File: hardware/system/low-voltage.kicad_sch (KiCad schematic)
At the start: 15 parts, among them M10 Buck 5 V >=2 A, M11 Motion carrier, M12 TB6600 1/8 step, M13 Stepper motor, M14 5 V relay module, M15 HOME bottom limit NC, M16 TOP limit NC, M17 Touch plate + clip on bit, M18 Foot pedal NO, M19 STOP flush NO, M20 Panel carrier, M21 Guition JC4827W543C, M22 MPG ZS80 100 PPR 5 V, M23 Panel buttons + rough/fine, M24 ROUTER LED

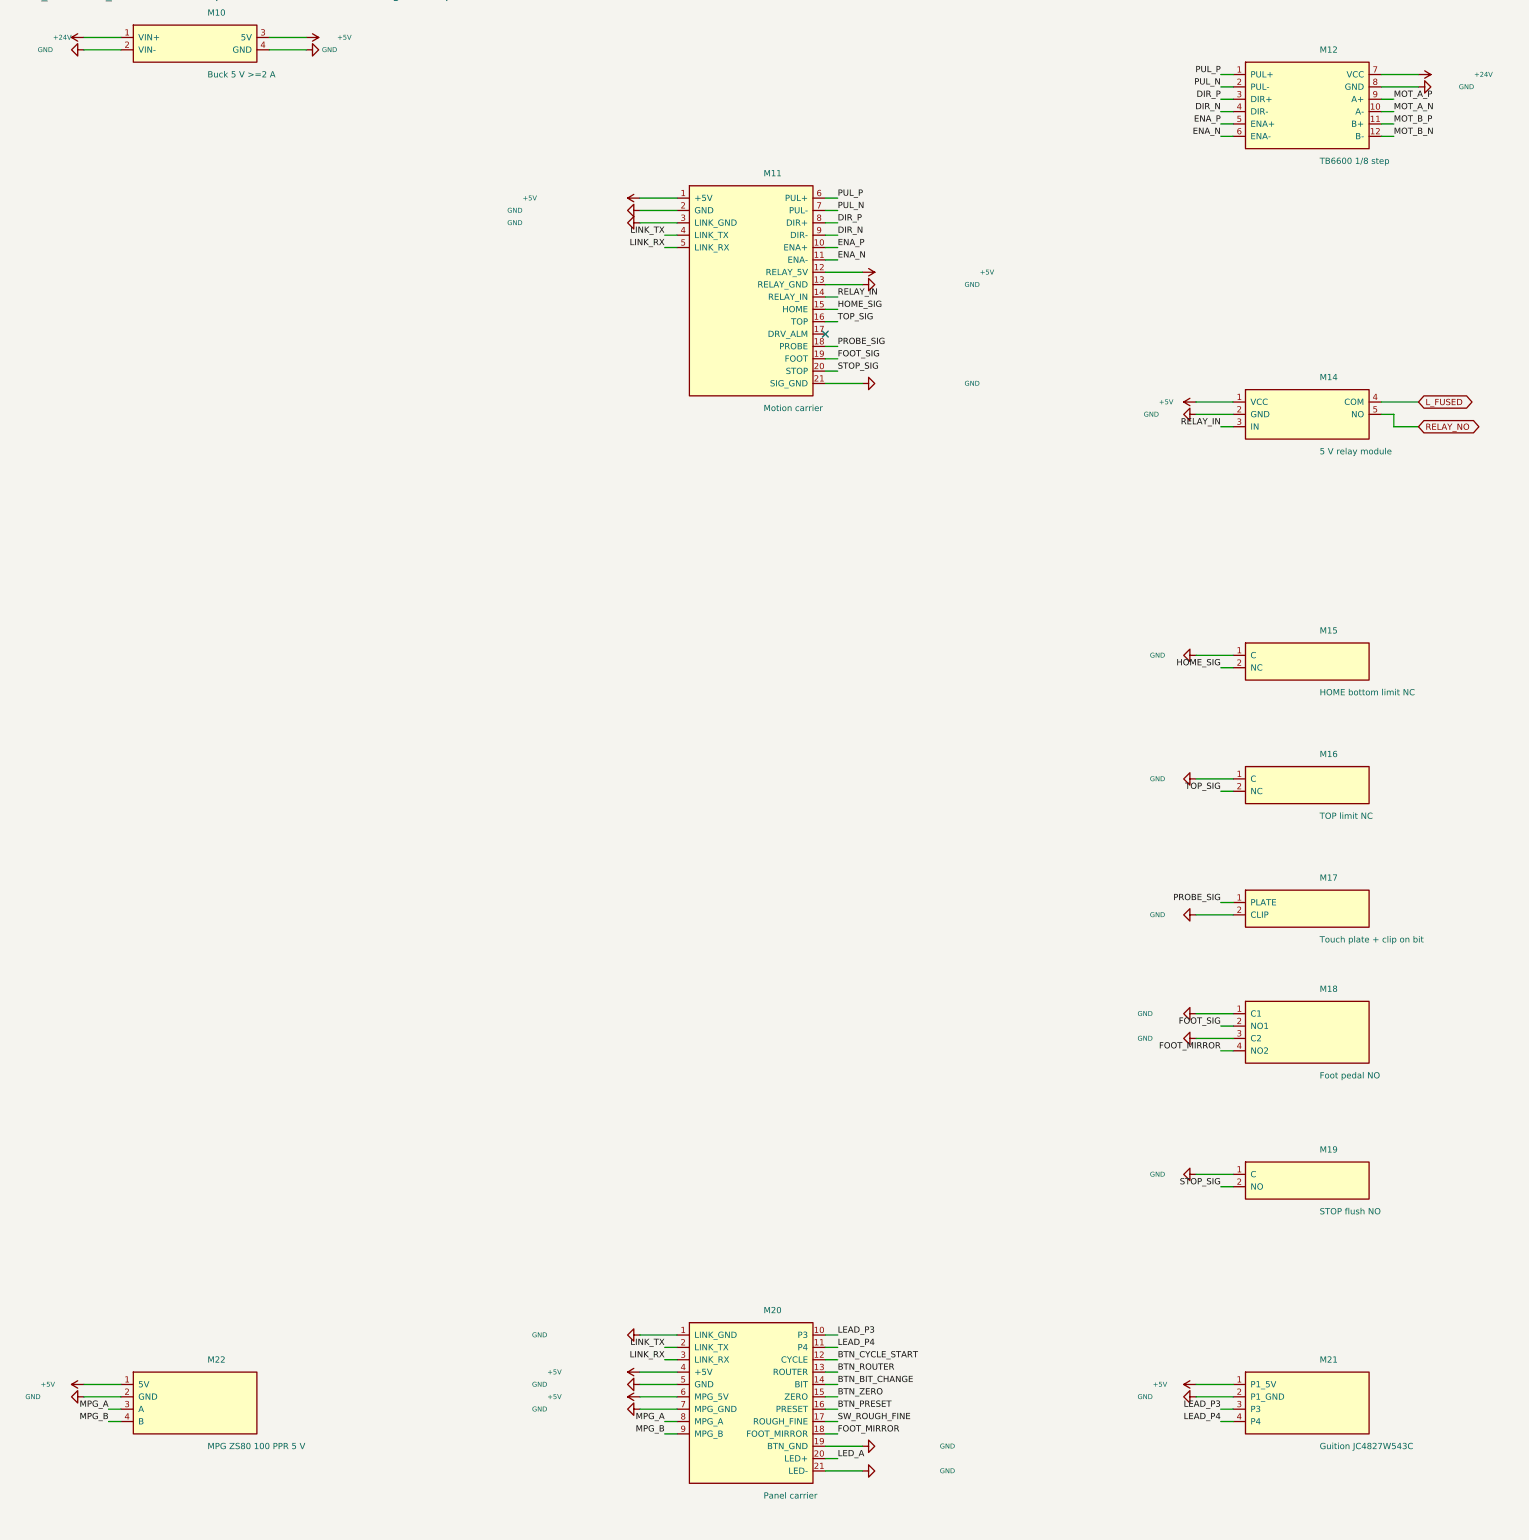
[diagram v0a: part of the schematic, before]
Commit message: fix(hardware): stop power-net arrows overlapping the plain pin below them
Review round 1 found a Critical, widespread legibility failure on the
low-voltage sheet: any box_symbol() row where a POWER_NET pin (GND/+5V) sits
directly above a plain-net pin had the plain label's text overlapped by the
power flag's own arrow/ground-symbol graphic, not just its Value text (already
covered by PowerNetLegibilityTest). Mechanism: the power flag's shape is
centred on its own row and reaches about half of box_symbol()'s 2.54mm row
pitch either side of it; a plain label is justified against the *bottom* of
its anchor (label()), so it grows upward, toward the row above. Both reaches
meet almost exactly at the row boundary by construction - stub length only
moves things along the wire, not perpendicular to it, so the earlier
"give globals the longer stub" fix could not touch this.

kisch.py: place() gains an opt-in `jog` parameter - {pin: extra} inserts a
perpendicular step into that one pin's wire before its label/flag. Every
existing caller that omits it draws the exact wire it always did (see
JogTest.test_omitting_jog_draws_the_same_single_straight_wire_as_before and
test_zero_jog_also_draws_a_single_straight_wire). Added JogTest: reproduces
the collision (both left- and right-side box_symbol() orientations, using the
real "power:GND" polyline geometry) and confirms a jog clears it.

hardware/tools/system.py: power_plain_jogs() computes the needed jog
automatically from BOXES + the nets being placed for every box - not
hand-tuned per occurrence. A power pin whose own row above is empty or plain
jogs itself up, away from the plain pin below. When its own above is another
power pin (no margin proven there to spare), the plain run below it - every
consecutive plain pin down to the next power pin or the end of the list -
cascades down together instead, preserving their mutual spacings exactly
while only shrinking the one gap already proven safe elsewhere in this file.
An earlier, si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
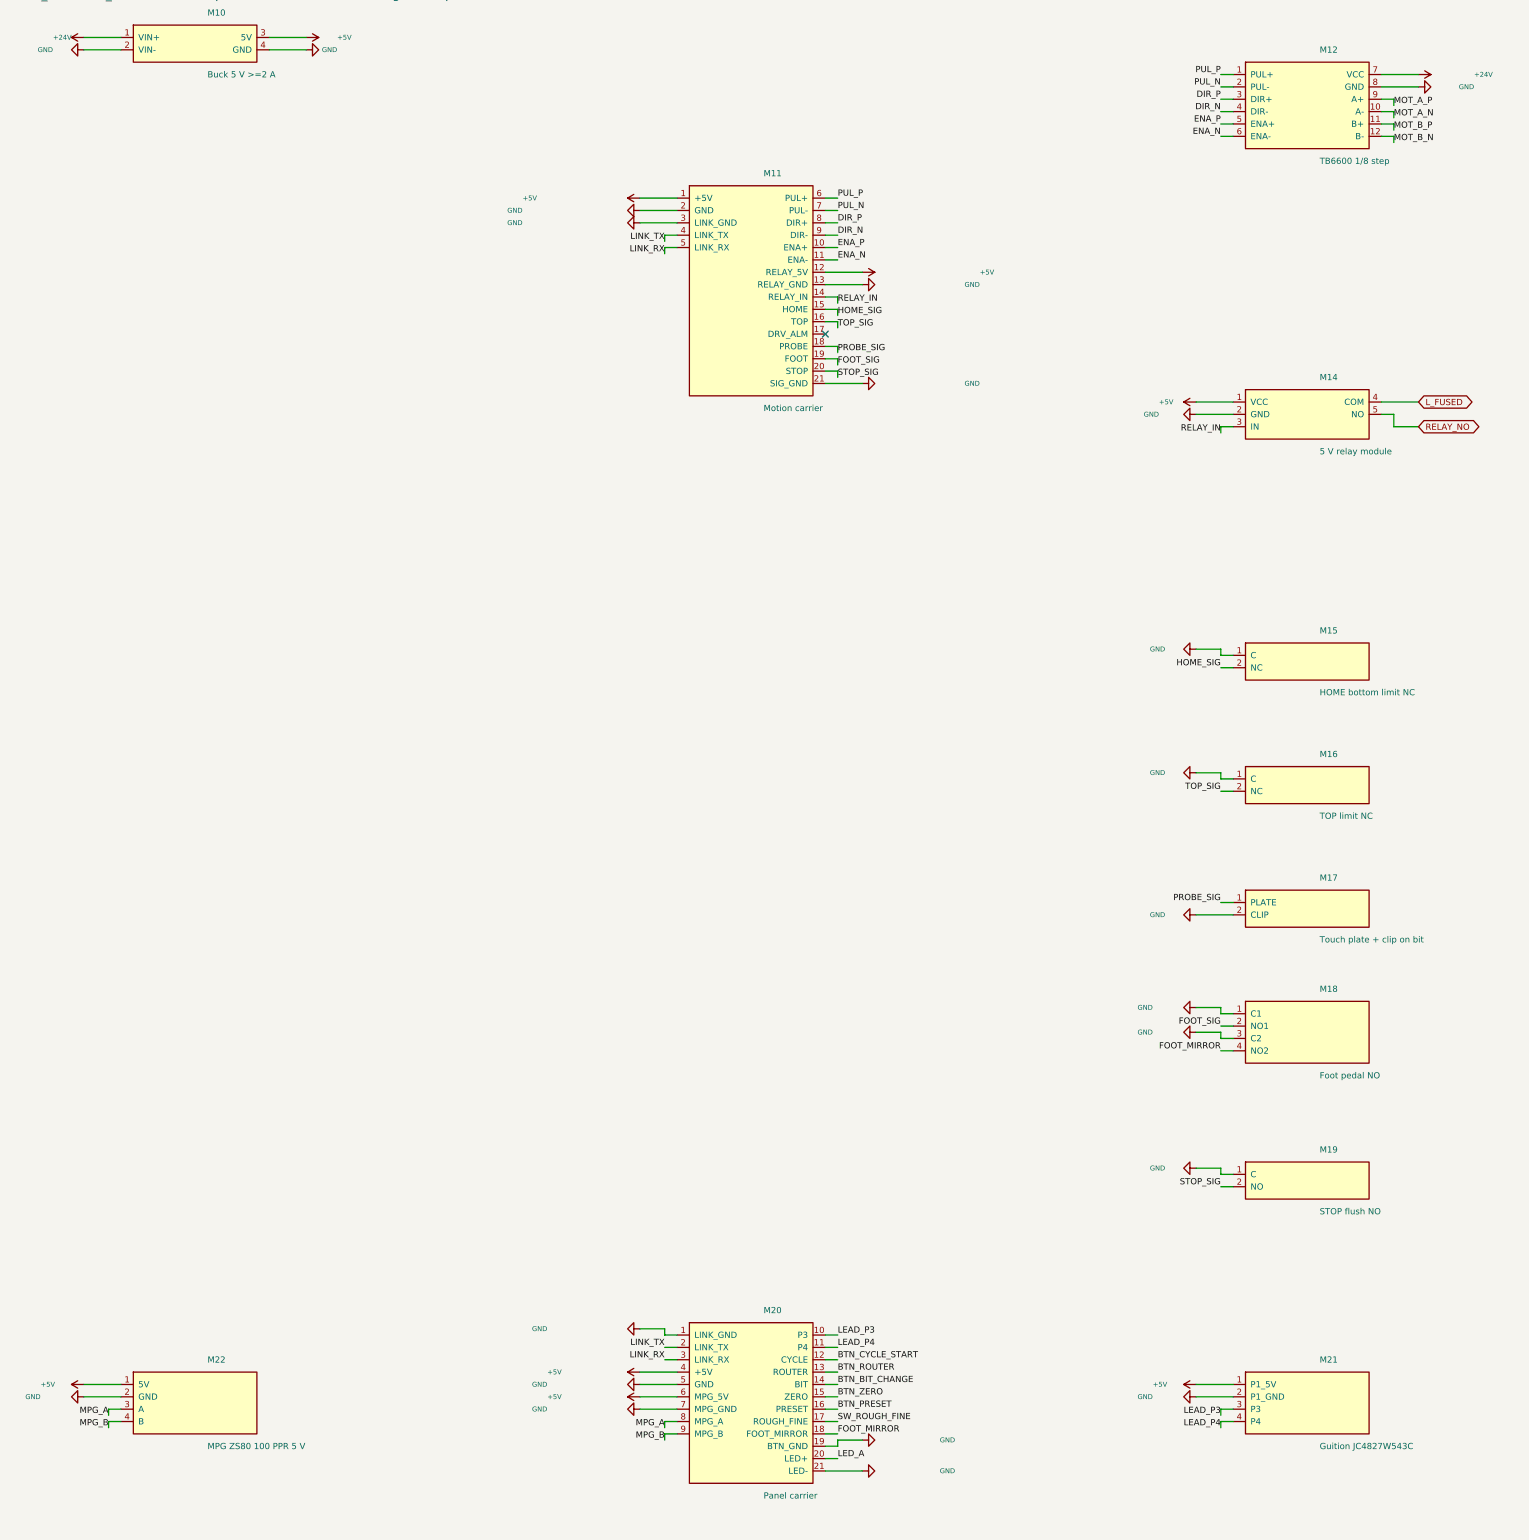
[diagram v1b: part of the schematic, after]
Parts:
- removed M13: Stepper motor, symbol routerlift:STEPPER
- added M19: STOP flush NO, symbol routerlift:STOP_BUTTON
- M13: renamed from M15; value HOME bottom limit NC -> Stepper motor; symbol routerlift:LIMIT_SWITCH_NC -> routerlift:STEPPER
- M15: renamed from M19; value STOP flush NO -> HOME bottom limit NC; symbol routerlift:STOP_BUTTON -> routerlift:LIMIT_SWITCH_NC
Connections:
- net GND: now also M19.1 (C); no longer M13.1 (C)
- net HOME_SIG: now also M15.2 (NC); no longer M13.2 (NC)
- net MOT_A_N: now also M13.2 (A-)
- net MOT_A_P: now also M13.1 (A+)
- net MOT_B_N: now also M13.4 (B-)
- net MOT_B_P: now also M13.3 (B+)
- net STOP_SIG: now also M19.2 (NO); no longer M15.2 (NO)
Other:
- moved on the sheet: M15

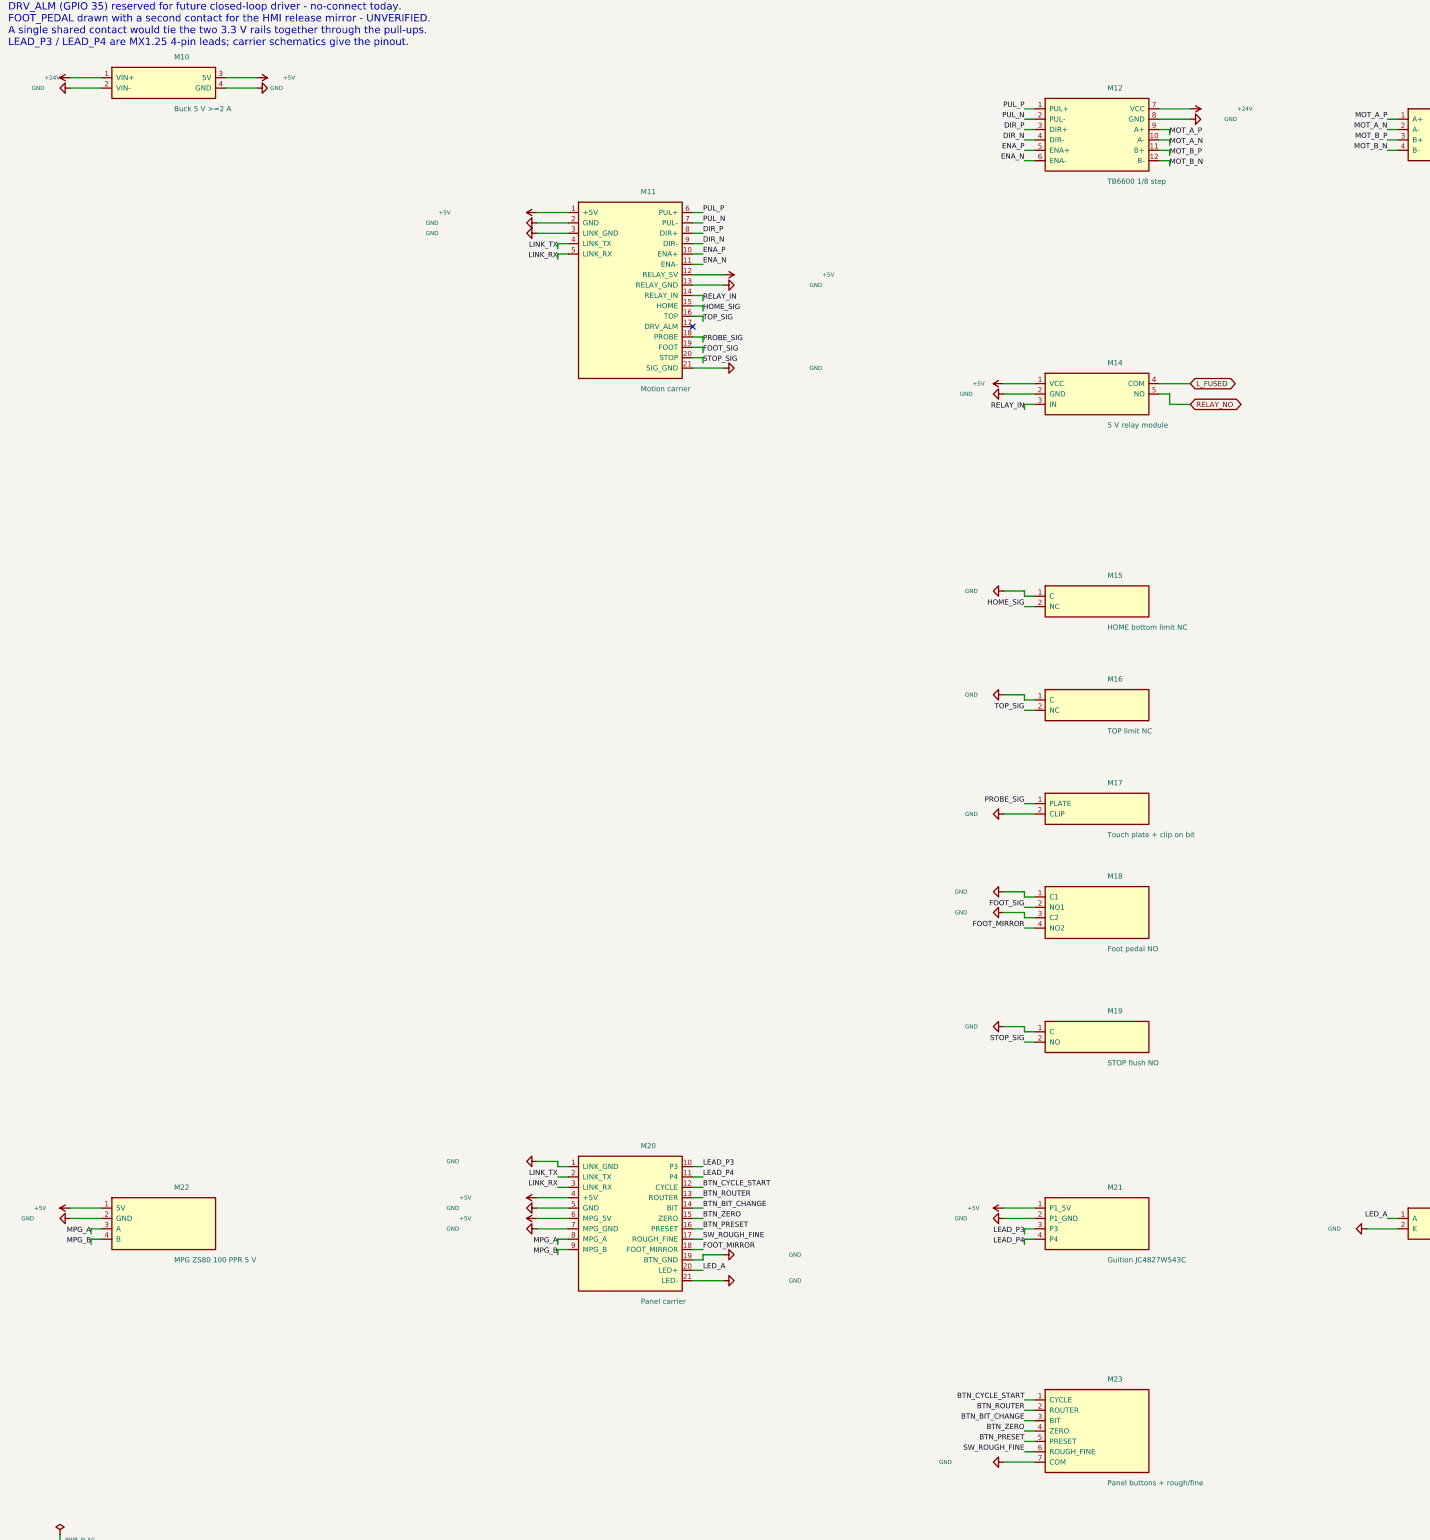
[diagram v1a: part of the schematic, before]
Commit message: fix(hardware): regenerate schematics, symbol library and PDFs
Regenerated output of the preceding fix-wave commits (contactor topology,
devkit pin order, field_gap/arrow-legibility fixes, 74LVC14 fields,
zero-length wire removal). ERC clean (0 violations on all three projects)
and check_pins reports 0 mismatches.

Co-Authored-By: Claude Opus 5 (1M context) <noreply@anthropic.com>
Claude-Session: https://claude.ai/code/session_01N1nWXzYgvFT6pqfHGhLK6P
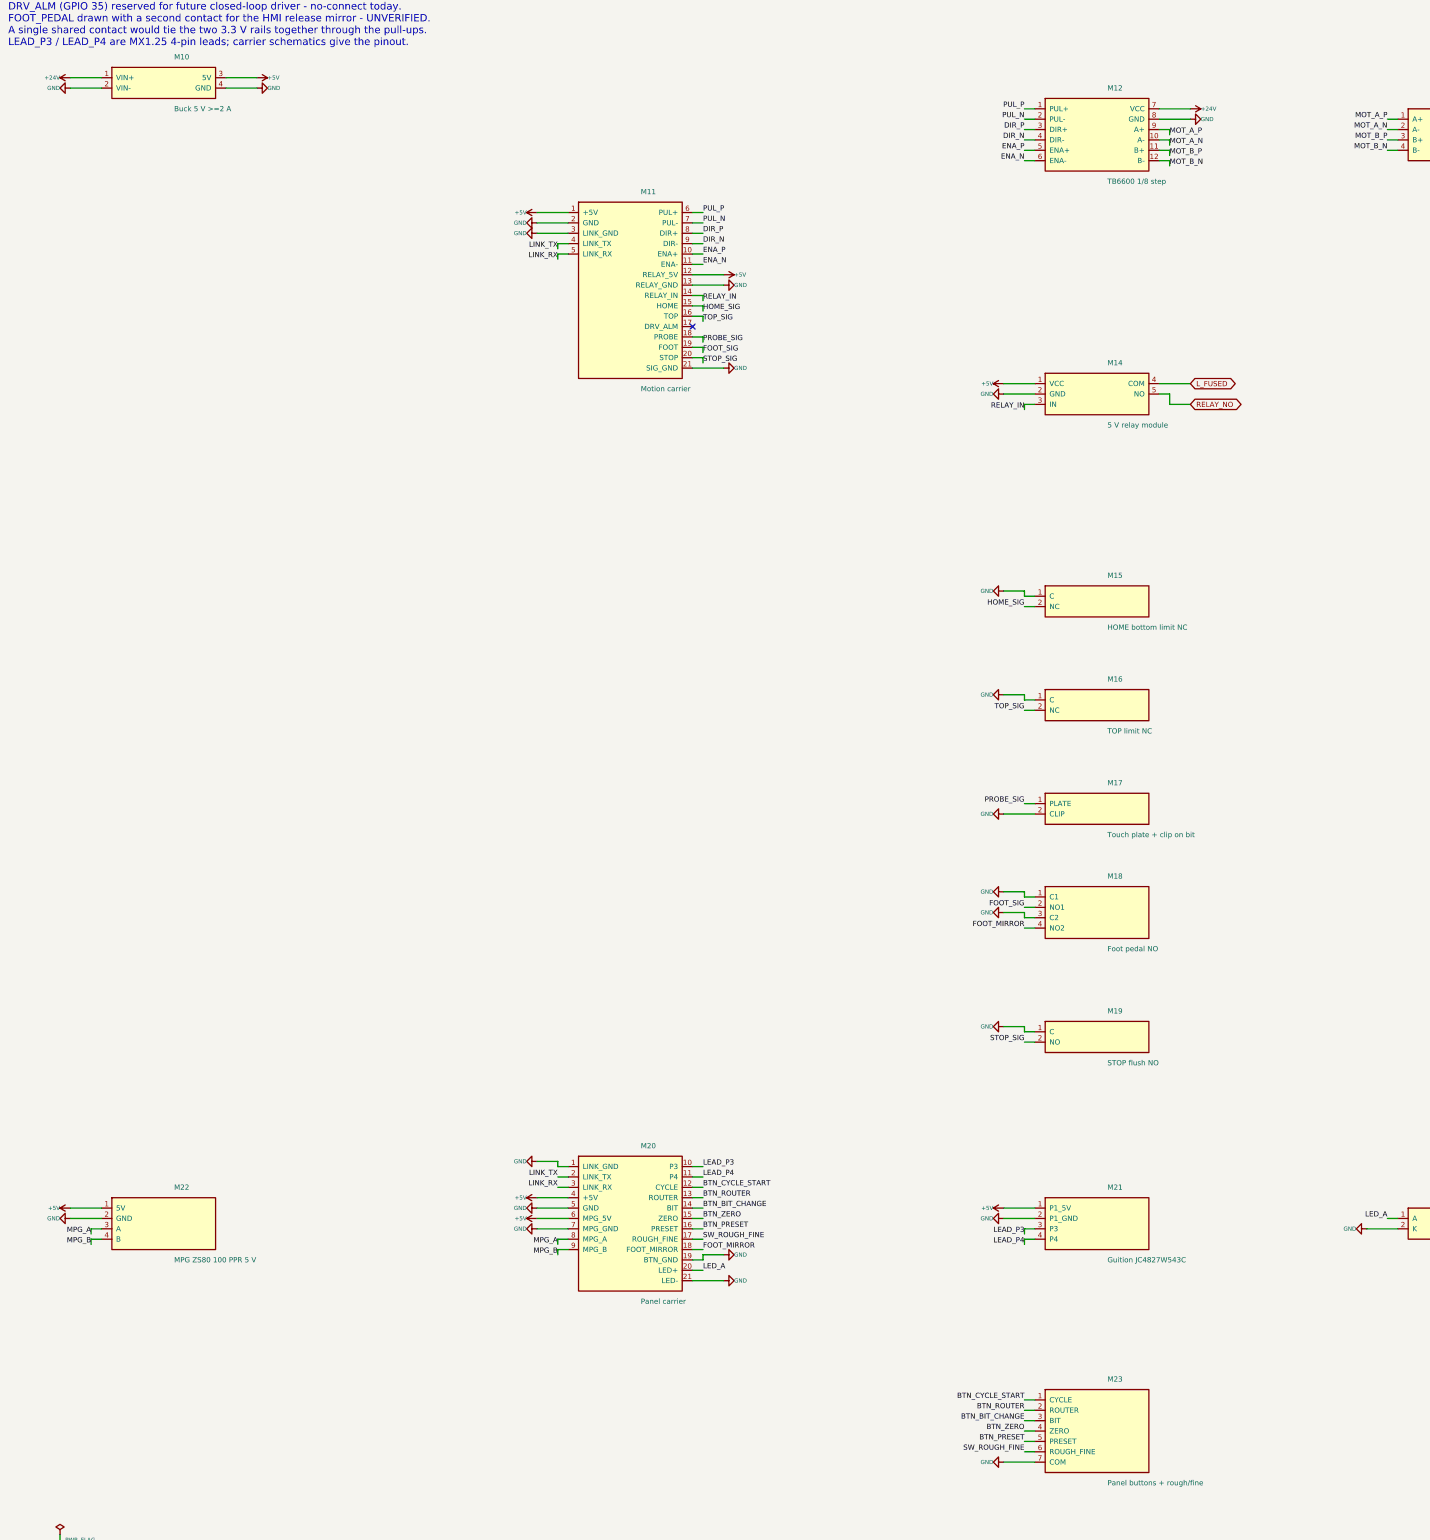
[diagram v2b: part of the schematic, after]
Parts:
- removed M19: STOP flush NO, symbol routerlift:STOP_BUTTON
- added M18: Foot pedal NO, symbol routerlift:FOOT_PEDAL
- M19: renamed from M18; value Foot pedal NO -> STOP flush NO; symbol routerlift:FOOT_PEDAL -> routerlift:STOP_BUTTON
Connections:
- net FOOT_MIRROR: now also M18.4 (NO2); no longer M19.4 (NO2)
- net FOOT_SIG: now also M18.2 (NO1); no longer M19.2 (NO1)
- net GND: now also M18.1 (C1), M18.3 (C2); no longer M19.3 (C2)
- net STOP_SIG: now also M19.2 (NO)
